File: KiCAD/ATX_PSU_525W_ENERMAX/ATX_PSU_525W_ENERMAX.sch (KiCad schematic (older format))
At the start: 0 parts

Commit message: moved all sub schematics to base schematic sheet due to minor complexity
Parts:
- added D? (x6): 20A, Diode_SMD_STMicroelectronics:DPAK228P972X240-3N, symbol Device:D_AAK
- added DZ? (x3): D_Zener, symbol Device:D_Zener
- added DZ? (x3): D_Zener_ALT, symbol Device:D_Zener_ALT
- added F? (x6): 10A, Fuse:Fuseholder_Cylinder-6.3x32mm_Schurter_0031-8002_Horizontal_Open, symbol Device:Fuse
- added J? (x3): Molex: 0039281243, Connector_Molex:Molex_Mini-Fit_Jr_5566-12A_2x06_P4.20mm_Vertical, symbol Connector_Generic:Conn_02x06_Counter_Clockwise
- added J?: Main ATX Conn. 02x12, Connector_Molex:Molex_Mini-Fit_Jr_5566-24A_2x12_P4.20mm_Vertical, symbol Connector_Generic:Conn_02x12_Counter_Clockwise
- added Q? (x3): Q_NMOS_DGS, Package_TO_SOT_THT:TO-220-3_Vertical, symbol Device:Q_NMOS_GDS
- added Q? (x3): Q_NMOS_GDS, symbol Device:Q_NMOS_GDS
- added R? (x6): 1M, Resistor_THT:R_Axial_DIN0516_L15.5mm_D5.0mm_P20.32mm_Horizontal, symbol Device:R
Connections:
- net labels added: +12V, +12V_OUT, +3.3V, +3.3V_IN, +3.3V_OUT, +5V, +5VSB, +5V_IN, +5V_OUT, -12V, GND, NC, PG, PS_ON
- wire segments 8 -> 169
- no-connect marks 2 -> 4
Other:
- note added: "Secondary Power Input"

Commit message: Redesign
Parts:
- removed D? (x6): 20A, Diode_SMD_STMicroelectronics:DPAK228P972X240-3N, symbol Device:D_AAK
- removed DZ? (x3): D_Zener, symbol Device:D_Zener
- removed DZ?: D_Zener_ALT, symbol Device:D_Zener_ALT
- removed F? (x3): 10A, Fuse:Fuseholder_Cylinder-6.3x32mm_Schurter_0031-8002_Horizontal_Open, symbol Device:Fuse
- removed J? (x2): Molex: 0039281243, Connector_Molex:Molex_Mini-Fit_Jr_5566-12A_2x06_P4.20mm_Vertical, symbol Connector_Generic:Conn_02x06_Counter_Clockwise
- removed Q? (x3): Q_NMOS_DGS, Package_TO_SOT_THT:TO-220-3_Vertical, symbol Device:Q_NMOS_GDS
- removed Q? (x3): Q_NMOS_GDS, symbol Device:Q_NMOS_GDS
- removed R? (x5): 1M, Resistor_THT:R_Axial_DIN0516_L15.5mm_D5.0mm_P20.32mm_Horizontal, symbol Device:R
- added DZ? (x3): D_Zener_ALT, symbol Device:D_Zener_ALT
- added F? (x2): 10A, Fuse:Fuseholder_Cylinder-6.3x32mm_Schurter_0031-8002_Horizontal_Open, symbol Device:Fuse
- added J? (x10): Conn_01x01, symbol Connector_Generic:Conn_01x01
- added J?: EPS12V 8 Pin, Connector_Molex:Molex_Mini-Fit_Jr_5566-12A_2x06_P4.20mm_Vertical, symbol Connector_Generic:Conn_02x04_Top_Bottom
- added J?: EPS12V 4Pin, symbol Connector_Generic:Conn_02x02_Top_Bottom
- added J? (x3): Molex: 0039281243, Connector_Molex:Molex_Mini-Fit_Jr_5566-08A2_2x04_P4.20mm_Vertical, symbol Connector_Generic:Conn_02x03_Counter_Clockwise
- added J? (x2): Molex: 0039281243, Connector_Molex:Molex_Mini-Fit_Jr_5566-12A_2x06_P4.20mm_Vertical, symbol Connector_Generic:Conn_02x06_Counter_Clockwise
- added J? (x4): Screw_Terminal_01x06, symbol Connector:Screw_Terminal_01x06
- added J?: Screw_Terminal_01x12, symbol Connector:Screw_Terminal_01x12
- added Q? (x5): Q_NMOS_DGS, Package_TO_SOT_THT:TO-220-3_Vertical, symbol Device:Q_NMOS_GDS
- added R? (x3): R, symbol Device:R
- added R? (x4): 1k, Resistor_THT:R_Axial_DIN0516_L15.5mm_D5.0mm_P20.32mm_Horizontal, symbol Device:R
- added RV? (x5): R_POT_Small, symbol Device:R_POT_Small
- J?: footprint Connector_Molex:Molex_Mini-Fit_Jr_5566-12A_2x06_P4.20mm_Vertical -> Connector_Molex:Molex_Mini-Fit_Jr_5566-08A2_2x04_P4.20mm_Vertical; symbol Connector_Generic:Conn_02x06_Counter_Clockwise -> Connector_Generic:Conn_02x03_Counter_Clockwise
- J?: value Main ATX Conn. 02x12 -> Main ATX 24Pin; symbol Connector_Generic:Conn_02x12_Counter_Clockwise -> Connector_Generic:Conn_02x12_Top_Bottom
- R?: value 1M -> 1k
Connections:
- net labels added: +12V1, +12V2, +12V3
- net labels removed: +12V_OUT, +3.3V_IN, +3.3V_OUT, +5V_IN, +5V_OUT
- wire segments 169 -> 165
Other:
- note added: "Negative Side"
- note added: "Positive Side"
- note added: "Primary +12V1 Power Rail Input"
- note added: "Secondary +12V2 Power Rail Input (MOLEX)"
- note added: "Secondary +12V2/+12V3 Power Rail Input (Screw Terminal)"
- note added: "Secondary +12V3 Power Rail Input (MOLEX)"
- note added: "Secondary +5V Power Input Terminal"
- note removed: "Secondary Power Input"
- moved on the sheet: DZ?, F?, R?

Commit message: labeling
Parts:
- J? (x3): value Conn_01x01 -> +12V Conn
- J?: value Conn_01x01 -> +5V Conn
- J?: value Conn_01x01 -> +3.3V Conn
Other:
- note added: "Income Current\nCircuit Protection"
- note added: "Return Current\nCurrent Regulation"
- note removed: "Negative Side"
- note removed: "Positive Side"

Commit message: bla
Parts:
- removed R? (x2): R, symbol Device:R
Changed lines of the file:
@@
-$EndComp
-$Comp
-L Device:R R?
-U 1 1 62704480
-P 5200 2250
-F 0 "R?" H 5270 2296 50  0000 L CNN
-F 1 "R" H 5270 2205 50  0000 L CNN
-F 2 "" V 5130 2250 50  0001 C CNN
-F 3 "~" H 5200 2250 50  0001 C CNN
-	1    5200 2250
-	1    0    0    -1
 $EndComp
 $Comp
@@
 	4950 2100 5200 2100
 Connection ~ 5200 2100
-$Comp
-L power:GNDREF #PWR?
-U 1 1 6270448E
-P 5200 2400
-F 0 "#PWR?" H 5200 2150 50  0001 C CNN
-F 1 "GNDREF" H 5205 2227 50  0000 C CNN
-F 2 "" H 5200 2400 50  0001 C CNN
-F 3 "" H 5200 2400 50  0001 C CNN
-	1    5200 2400
-	1    0    0    -1
-$EndComp
 Text GLabel 4950 2100 0    50   Input ~ 0
 +12V2
@@
 $EndComp
 $Comp
-L Device:R R?
-U 1 1 62714697
-P 5200 3250
-F 0 "R?" H 5270 3296 50  0000 L CNN
-F 1 "R" H 5270 3205 50  0000 L CNN
-F 2 "" V 5130 3250 50  0001 C CNN
-F 3 "~" H 5200 3250 50  0001 C CNN
-	1    5200 3250
-	1    0    0    -1
-$EndComp
-$Comp
 L power:+12V #PWR?
 U 1 1 6271469D
@@
 	4950 3100 5200 3100
 Connection ~ 5200 3100
-$Comp
-L power:GNDREF #PWR?
-U 1 1 627146A5
-P 5200 3400
-F 0 "#PWR?" H 5200 3150 50  0001 C CNN
-F 1 "GNDREF" H 5205 3227 50  0000 C CNN
-F 2 "" H 5200 3400 50  0001 C CNN
-F 3 "" H 5200 3400 50  0001 C CNN
-	1    5200 3400
-	1    0    0    -1
-$EndComp
 Text GLabel 4950 3100 0    50   Input ~ 0
 +12V3

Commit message: bla
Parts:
- removed J?: +12V Conn, symbol Connector_Generic:Conn_01x01
- removed J?: Conn_01x01, symbol Connector_Generic:Conn_01x01
- removed Q?: Q_NMOS_DGS, Package_TO_SOT_THT:TO-220-3_Vertical, symbol Device:Q_NMOS_GDS
- removed R?: 1k, Resistor_THT:R_Axial_DIN0516_L15.5mm_D5.0mm_P20.32mm_Horizontal, symbol Device:R
- removed RV?: R_POT_Small, symbol Device:R_POT_Small
- added C?: 1nF, symbol Device:C
- added C?: 0.1uF, symbol Device:C
- added HS?: Heatsink, symbol Mechanical:Heatsink_Pad
- added J?: Conn Potti, Connector_Molex:Molex_KK-254_AE-6410-03A_1x03_P2.54mm_Vertical, symbol Connector_Generic:Conn_01x03
- added J?: Current Sens, Connector_Molex:Molex_KK-254_AE-6410-03A_1x03_P2.54mm_Vertical, symbol Connector_Generic:Conn_01x03
- added J?: Volt Sens, Connector_Molex:Molex_KK-254_AE-6410-02A_1x02_P2.54mm_Vertical, symbol Connector_Generic:Conn_01x02
- added J?: 12V Out, symbol Connector:Screw_Terminal_01x02
- added J?: Fan1, Connector_Molex:Molex_KK-254_AE-6410-02A_1x02_P2.54mm_Vertical, symbol Connector_Generic:Conn_01x02
- added LA?: PWR Indicator, symbol Device:Lamp
- added Q?: Q_NMOS_DGS, Package_TO_SOT_THT:TO-220-3_Vertical, symbol Device:Q_NMOS_GDS
- added R?: 1k, Resistor_THT:R_Axial_DIN0516_L15.5mm_D5.0mm_P20.32mm_Horizontal, symbol Device:R
- added U?: ACS712xLCTR-20A, Package_SO:SOIC-8_3.9x4.9mm_P1.27mm, symbol Sensor_Current:ACS712xLCTR-20A
- R?: footprint (none) -> Resistor_THT:R_Axial_Power_L20.0mm_W6.4mm_P25.40mm
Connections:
- net +12V: now also DZ?.1 (K), F?.2, J?.1 (Pin_1), R?.2, U?.1 (IP+), U?.2 (IP+); no longer F?.1, J?.10 (Pin_10), J?.11 (Pin_11), J?.3 (Pin_3), J?.4 (Pin_4), J?.5 (Pin_5), J?.6 (Pin_6), J?.7 (Pin_7), J?.8 (Pin_8)
- net +5V: now also C?.2, J?.1 (Pin_1), U?.8 (VCC)
- net GNDREF: now also C?.1, C?.1, HS?.1, J?.3 (Pin_3), J?.3 (Pin_3), LA?.1 (-), Q?.3 (S), U?.5 (GND); no longer R?.2
- new net: LA?.2 (+), R?.2
- new net: J?.1 (Pin_1), R?.1
- new net: J?.2 (Pin_2), Q?.1 (G)
- new net: J?.1 (Pin_1), J?.1 (Pin_1), U?.3 (IP-), U?.4 (IP-)
- new net: C?.2, U?.6 (FILTER)
- new net: J?.2 (Pin_2), U?.7 (VIOUT)
- new net +12V1: F?.1, J?.10 (Pin_10), J?.11 (Pin_11), J?.3 (Pin_3), J?.4 (Pin_4), J?.5 (Pin_5), J?.6 (Pin_6), J?.7 (Pin_7), J?.8 (Pin_8)
- new net 12V1-: J?.2 (Pin_2), J?.2 (Pin_2), J?.2 (Pin_2), Q?.2 (D)
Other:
- note removed: "Income Current\nCircuit Protection"
- note removed: "Return Current\nCurrent Regulation"
- moved on the sheet: DZ?, F?, J?, Q?, R?, RV?

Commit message: blub
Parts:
- removed DZ? (x4): D_Zener_ALT, symbol Device:D_Zener_ALT
- removed F? (x4): 10A, Fuse:Fuseholder_Cylinder-6.3x32mm_Schurter_0031-8002_Horizontal_Open, symbol Device:Fuse
- removed J?: +5V Conn, symbol Connector_Generic:Conn_01x01
- removed J?: +3.3V Conn, symbol Connector_Generic:Conn_01x01
- removed J? (x4): Conn_01x01, symbol Connector_Generic:Conn_01x01
- removed J? (x2): +12V Conn, symbol Connector_Generic:Conn_01x01
- removed Q? (x4): Q_NMOS_DGS, Package_TO_SOT_THT:TO-220-3_Vertical, symbol Device:Q_NMOS_GDS
- removed R? (x4): 1k, Resistor_THT:R_Axial_DIN0516_L15.5mm_D5.0mm_P20.32mm_Horizontal, symbol Device:R
- removed RV? (x4): R_POT_Small, symbol Device:R_POT_Small
- added C? (x4): 0.1uF, symbol Device:C
- added C? (x4): 1nF, symbol Device:C
- added DZ? (x4): D_Zener_ALT, symbol Device:D_Zener_ALT
- added F? (x4): 10A, Fuse:Fuseholder_Cylinder-6.3x32mm_Schurter_0031-8002_Horizontal_Open, symbol Device:Fuse
- added HS? (x4): Heatsink, Heatsink:Heatsink_Stonecold_HS-132_32x14mm_2xFixation1.5mm, symbol Mechanical:Heatsink_Pad
- added J? (x4): Current Sens, Connector_Molex:Molex_KK-254_AE-6410-03A_1x03_P2.54mm_Vertical, symbol Connector_Generic:Conn_01x03
- added J? (x2): 12V Out, TerminalBlock_Altech:Altech_AK300_1x02_P5.00mm_45-Degree, symbol Connector:Screw_Terminal_01x02
- added J? (x4): Volt Sens, Connector_Molex:Molex_KK-254_AE-6410-02A_1x02_P2.54mm_Vertical, symbol Connector_Generic:Conn_01x02
- added J? (x4): Fan1, Connector_Molex:Molex_KK-254_AE-6410-02A_1x02_P2.54mm_Vertical, symbol Connector_Generic:Conn_01x02
- added J? (x4): Potti, Connector_Molex:Molex_KK-254_AE-6410-03A_1x03_P2.54mm_Vertical, symbol Connector_Generic:Conn_01x03
- added J?: 5V Out, TerminalBlock_Altech:Altech_AK300_1x02_P5.00mm_45-Degree, symbol Connector:Screw_Terminal_01x02
- added J?: 3.3V Out, TerminalBlock_Altech:Altech_AK300_1x02_P5.00mm_45-Degree, symbol Connector:Screw_Terminal_01x02
- added Q? (x4): Q_NMOS_DGS, Package_TO_SOT_THT:TO-220-3_Vertical, symbol Device:Q_NMOS_GDS
- added R? (x4): 1k, Resistor_THT:R_Axial_DIN0516_L15.5mm_D5.0mm_P20.32mm_Horizontal, symbol Device:R
- added U? (x4): ACS712xLCTR-20A, Package_SO:SOIC-8_3.9x4.9mm_P1.27mm, symbol Sensor_Current:ACS712xLCTR-20A
- HS?: footprint (none) -> Heatsink:Heatsink_Stonecold_HS-132_32x14mm_2xFixation1.5mm
- J?: value Conn Potti -> Potti
- J?: footprint (none) -> TerminalBlock_Altech:Altech_AK300_1x02_P5.00mm_45-Degree
- LA?: footprint (none) -> LED_THT:LED_D4.0mm
- R?: value R -> 20
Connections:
- net +12V: now also DZ?.1 (K), DZ?.1 (K), F?.2, F?.2, J?.1 (Pin_1), J?.1 (Pin_1), R?.2, R?.2, U?.1 (IP+), U?.1 (IP+), U?.2 (IP+), U?.2 (IP+); no longer J?.1 (Pin_1), J?.1 (Pin_1), J?.10 (Pin_10), J?.10 (Pin_10), J?.11 (Pin_11), J?.11 (Pin_11), J?.12 (Pin_12), J?.12 (Pin_12), J?.2 (Pin_2), J?.2 (Pin_2), J?.3 (Pin_3), J?.3 (Pin_3), J?.4 (Pin_4), J?.4 (Pin_4), J?.4 (Pin_4), J?.4 (Pin_4), J?.4 (Pin_4), J?.4 (Pin_4), J?.5 (Pin_5), J?.5 (Pin_5), J?.5 (Pin_5), J?.5 (Pin_5), J?.5 (Pin_5), J?.5 (Pin_5), J?.6 (Pin_6), J?.6 (Pin_6), J?.6 (Pin_6), J?.6 (Pin_6), J?.6 (Pin_6), J?.6 (Pin_6), J?.7 (Pin_7), J?.7 (Pin_7), J?.8 (Pin_8), J?.8 (Pin_8), J?.9 (Pin_9), J?.9 (Pin_9)
- net +3V3: now also DZ?.1 (K), F?.2, J?.1 (Pin_1), R?.2, U?.1 (IP+), U?.2 (IP+); no longer J?.1 (Pin_1), J?.1 (Pin_1), J?.12 (Pin_12), J?.13 (Pin_13), J?.2 (Pin_2), J?.2 (Pin_2), J?.3 (Pin_3), J?.4 (Pin_4), J?.5 (Pin_5), J?.6 (Pin_6)
- net +5V: now also C?.2, C?.2, C?.2, C?.2, DZ?.1 (K), F?.1, F?.2, J?.1 (Pin_1), J?.1 (Pin_1), J?.1 (Pin_1), J?.1 (Pin_1), J?.1 (Pin_1), R?.2, U?.1 (IP+), U?.2 (IP+), U?.8 (VCC), U?.8 (VCC), U?.8 (VCC), U?.8 (VCC)
- net 12V1-: no longer J?.2 (Pin_2)
- net GNDREF: now also J?.2 (Pin_2), R?.2, C?.1, C?.1, C?.1, C?.1, C?.1, C?.1, C?.1, C?.1, DZ?.2 (A), DZ?.2 (A), DZ?.2 (A), DZ?.2 (A), HS?.1, HS?.1, HS?.1, HS?.1, J?.2 (Pin_2), J?.2 (Pin_2), J?.2 (Pin_2), J?.2 (Pin_2), J?.3 (Pin_3), J?.3 (Pin_3), J?.3 (Pin_3), J?.3 (Pin_3), J?.3 (Pin_3), J?.3 (Pin_3), J?.3 (Pin_3), J?.3 (Pin_3), Q?.3 (S), Q?.3 (S), Q?.3 (S), Q?.3 (S), U?.5 (GND), U?.5 (GND), U?.5 (GND), U?.5 (GND); no longer LA?.1 (-)
- net at LA?.2 (+): no longer R?.2
- new net: J?.2 (Pin_2), Q?.1 (G) (x4)
- new net: J?.2 (Pin_2), U?.7 (VIOUT) (x4)
- new net: C?.2, U?.6 (FILTER) (x4)
- new net: J?.1 (Pin_1), J?.1 (Pin_1), U?.3 (IP-), U?.4 (IP-) (x4)
- new net: J?.1 (Pin_1), R?.1 (x4)
- new net +12V2: F?.1, J?.1 (Pin_1), J?.10 (Pin_10), J?.11 (Pin_11), J?.12 (Pin_12), J?.2 (Pin_2), J?.3 (Pin_3), J?.4 (Pin_4), J?.4 (Pin_4), J?.4 (Pin_4), J?.5 (Pin_5), J?.5 (Pin_5), J?.5 (Pin_5), J?.6 (Pin_6), J?.6 (Pin_6), J?.6 (Pin_6), J?.7 (Pin_7), J?.8 (Pin_8), J?.9 (Pin_9)
- new net +12V3: F?.1, J?.1 (Pin_1), J?.10 (Pin_10), J?.11 (Pin_11), J?.12 (Pin_12), J?.2 (Pin_2), J?.3 (Pin_3), J?.4 (Pin_4), J?.4 (Pin_4), J?.4 (Pin_4), J?.5 (Pin_5), J?.5 (Pin_5), J?.5 (Pin_5), J?.6 (Pin_6), J?.6 (Pin_6), J?.6 (Pin_6), J?.7 (Pin_7), J?.8 (Pin_8), J?.9 (Pin_9)
- new net +3.3V: F?.1, J?.1 (Pin_1), J?.1 (Pin_1), J?.12 (Pin_12), J?.13 (Pin_13), J?.2 (Pin_2), J?.2 (Pin_2), J?.3 (Pin_3), J?.4 (Pin_4), J?.5 (Pin_5), J?.6 (Pin_6)
- new net 12V2-: J?.2 (Pin_2), J?.2 (Pin_2), Q?.2 (D)
- new net 12V3-: J?.2 (Pin_2), J?.2 (Pin_2), Q?.2 (D)
- new net 3.3V-: J?.2 (Pin_2), J?.2 (Pin_2), Q?.2 (D)
- new net 5V-: J?.2 (Pin_2), J?.2 (Pin_2), Q?.2 (D)
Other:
- moved on the sheet: C?, DZ?, F?, HS?, J?, LA?, Q?, R?, U?

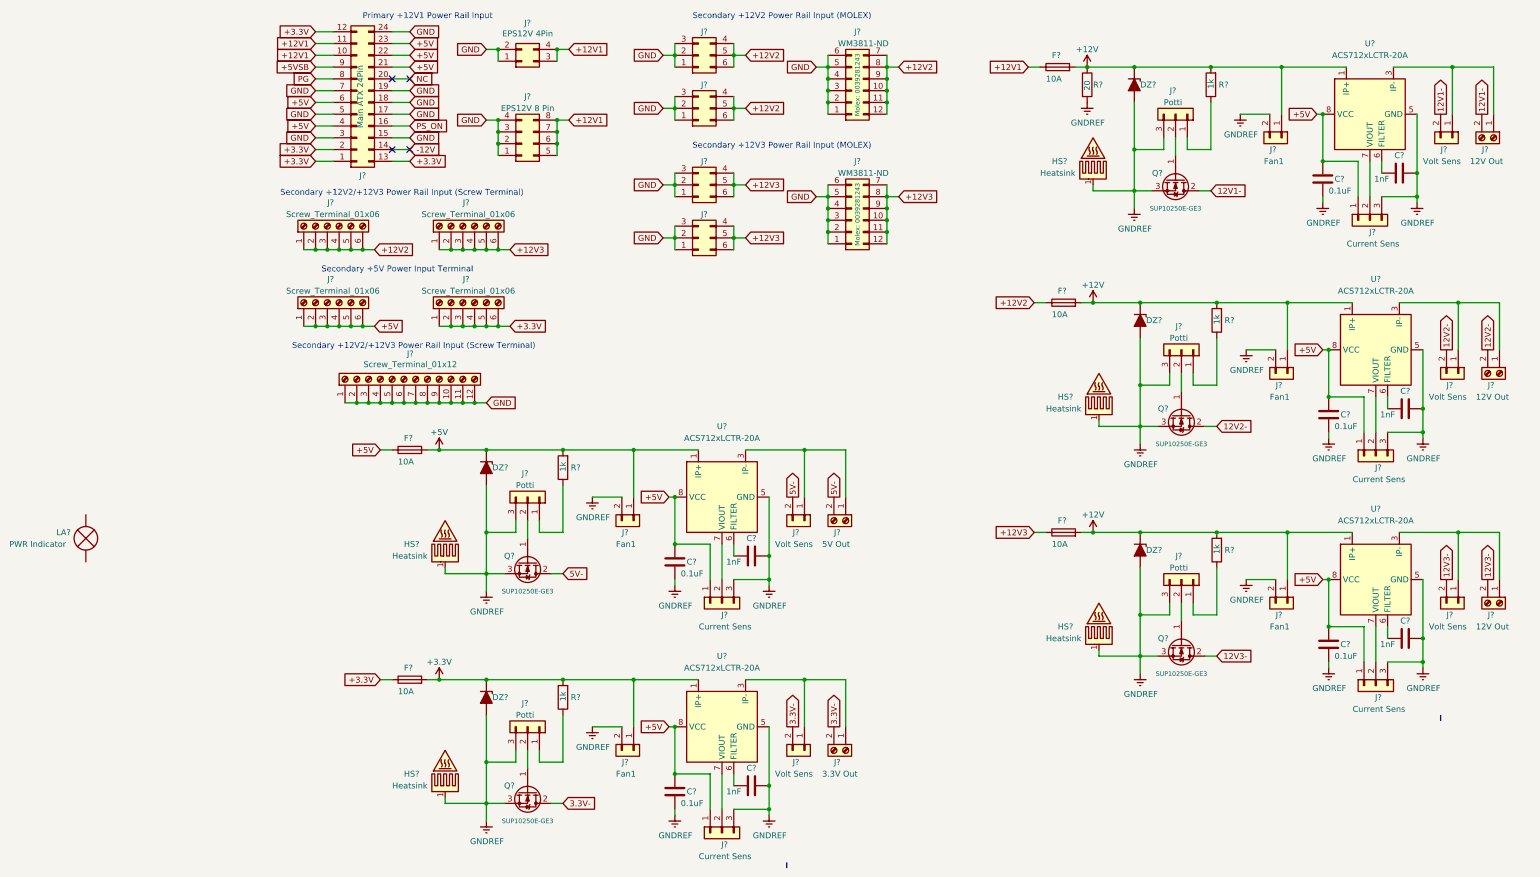
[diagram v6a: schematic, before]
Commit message: Finalizing and labeling schematics
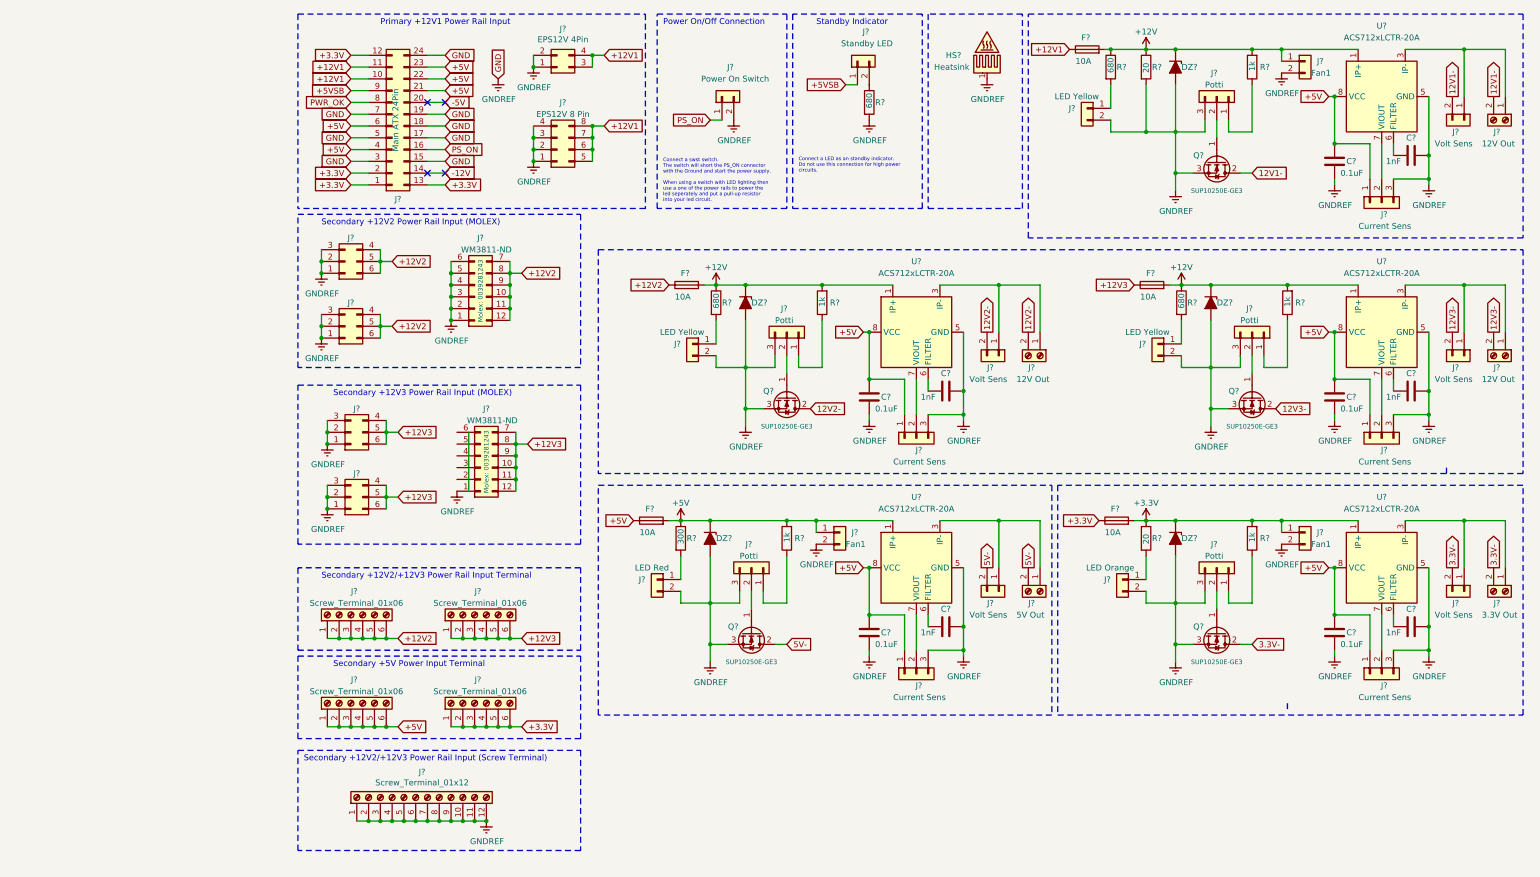
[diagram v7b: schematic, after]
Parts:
- removed HS? (x4): Heatsink, Heatsink:Heatsink_Stonecold_HS-132_32x14mm_2xFixation1.5mm, symbol Mechanical:Heatsink_Pad
- removed J? (x4): Fan1, Connector_Molex:Molex_KK-254_AE-6410-02A_1x02_P2.54mm_Vertical, symbol Connector_Generic:Conn_01x02
- removed LA?: PWR Indicator, LED_THT:LED_D4.0mm, symbol Device:Lamp
- added J? (x2): Fan1, Connector_Molex:Molex_KK-254_AE-6410-02A_1x02_P2.54mm_Vertical, symbol Connector_Generic:Conn_01x02
- added J? (x3): LED Yellow, Connector_Molex:Molex_KK-254_AE-6410-02A_1x02_P2.54mm_Vertical, symbol Connector_Generic:Conn_01x02
- added J?: LED Red, Connector_Molex:Molex_KK-254_AE-6410-02A_1x02_P2.54mm_Vertical, symbol Connector_Generic:Conn_01x02
- added J?: LED Orange, Connector_Molex:Molex_KK-254_AE-6410-02A_1x02_P2.54mm_Vertical, symbol Connector_Generic:Conn_01x02
- added J?: Power On Switch, Connector_Molex:Molex_KK-254_AE-6410-02A_1x02_P2.54mm_Vertical, symbol Connector_Generic:Conn_01x02
- added J?: Standby LED, Connector_Molex:Molex_KK-254_AE-6410-02A_1x02_P2.54mm_Vertical, symbol Connector_Generic:Conn_01x02
- added R? (x4): 680, Resistor_THT:R_Axial_Power_L20.0mm_W6.4mm_P25.40mm, symbol Device:R
- added R?: 300, Resistor_THT:R_Axial_Power_L20.0mm_W6.4mm_P25.40mm, symbol Device:R
- added R?: 20, Resistor_THT:R_Axial_Power_L20.0mm_W6.4mm_P25.40mm, symbol Device:R
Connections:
- net +12V: now also J?.1 (Pin_1), R?.1, R?.1, R?.1
- net +3V3: now also J?.1 (Pin_1), R?.1
- net +5V: now also R?.1
- net +5VSB: now also J?.1 (Pin_1)
- net GNDREF: now also J?.1 (Pin_1), J?.1 (Pin_1), J?.1 (Pin_1), J?.1 (Pin_1), J?.1 (Pin_1), J?.1 (Pin_1), J?.1 (Pin_1), J?.1 (Pin_1), J?.1 (Pin_1), J?.10 (Pin_10), J?.11 (Pin_11), J?.12 (Pin_12), J?.15 (Pin_15), J?.17 (Pin_17), J?.18 (Pin_18), J?.19 (Pin_19), J?.2 (Pin_2), J?.2 (Pin_2), J?.2 (Pin_2), J?.2 (Pin_2), J?.2 (Pin_2), J?.2 (Pin_2), J?.2 (Pin_2), J?.2 (Pin_2), J?.24 (Pin_24), J?.3 (Pin_3), J?.3 (Pin_3), J?.3 (Pin_3), J?.3 (Pin_3), J?.3 (Pin_3), J?.3 (Pin_3), J?.3 (Pin_3), J?.3 (Pin_3), J?.4 (Pin_4), J?.4 (Pin_4), J?.4 (Pin_4), J?.5 (Pin_5), J?.5 (Pin_5), J?.5 (Pin_5), J?.6 (Pin_6), J?.6 (Pin_6), J?.7 (Pin_7), J?.7 (Pin_7), J?.8 (Pin_8), J?.9 (Pin_9), J?.2 (Pin_2), J?.2 (Pin_2), J?.2 (Pin_2), J?.2 (Pin_2), J?.2 (Pin_2), J?.2 (Pin_2), J?.2 (Pin_2), J?.2 (Pin_2), R?.2
- net PS_ON: now also J?.1 (Pin_1)
- removed net GND: J?.1 (Pin_1), J?.1 (Pin_1), J?.1 (Pin_1), J?.1 (Pin_1), J?.1 (Pin_1), J?.1 (Pin_1), J?.1 (Pin_1), J?.1 (Pin_1), J?.1 (Pin_1), J?.10 (Pin_10), J?.11 (Pin_11), J?.12 (Pin_12), J?.15 (Pin_15), J?.17 (Pin_17), J?.18 (Pin_18), J?.19 (Pin_19), J?.2 (Pin_2), J?.2 (Pin_2), J?.2 (Pin_2), J?.2 (Pin_2), J?.2 (Pin_2), J?.2 (Pin_2), J?.2 (Pin_2), J?.2 (Pin_2), J?.2 (Pin_2), J?.24 (Pin_24), J?.3 (Pin_3), J?.3 (Pin_3), J?.3 (Pin_3), J?.3 (Pin_3), J?.3 (Pin_3), J?.3 (Pin_3), J?.3 (Pin_3), J?.3 (Pin_3), J?.3 (Pin_3), J?.4 (Pin_4), J?.4 (Pin_4), J?.4 (Pin_4), J?.4 (Pin_4), J?.5 (Pin_5), J?.5 (Pin_5), J?.5 (Pin_5), J?.5 (Pin_5), J?.6 (Pin_6), J?.6 (Pin_6), J?.6 (Pin_6), J?.7 (Pin_7), J?.7 (Pin_7), J?.8 (Pin_8), J?.9 (Pin_9)
- net NC renamed -5V
- net PG renamed PWR_OK
- new net: J?.1 (Pin_1), R?.2 (x5)
- new net: J?.2 (Pin_2), R?.1
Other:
- note added: "Connect a LED as an standby indicator.\nDo not use this connection for high power \ncircuits."
- note added: "Connect a swst switch.\nThe switch will short the PS_ON connector \nwith the Ground and start the power supply.\n\nWhen using a switch with LED lighting then\nuse a one of the power rails to power the\nled seperately and put a pull-up resistor\ninto your led circuit."
- note added: "Power On/Off Connection"
- note added: "Secondary +12V2/+12V3 Power Rail Input Terminal"
- note added: "Standby Indicator"
- moved on the sheet: C?, DZ?, F?, HS?, J?, Q?, R?, U?
